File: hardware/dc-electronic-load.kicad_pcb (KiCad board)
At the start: 2 copper layers, 4 parts, among them M1 Mounting Hole, M2 Mounting Hole, M3 Mounting Hole, M4 Mounting Hole

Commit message: more module assigning
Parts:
- added C1: 18pF, klib:CAPC2012X100N, F.Cu at (175.9, 88.4)
- added C10: 0.1uF, klib:CAPC2012X100N, F.Cu at (162.2, 100.4)
- added C11: 0.1uF, klib:CAPC2012X100N, F.Cu at (185.7, 83.4)
- added C12: 0.1uF, klib:CAPC2012X100N, F.Cu at (190.7, 79.1)
- added C13: 0.47uF, klib:CAPC2012X100N, F.Cu at (195.7, 74.0)
- added C14: 0.1uF, klib:CAPC2012X100N, F.Cu at (162.2, 97.8)
- added C15: 0.1uF, klib:CAPC2012X100N, F.Cu at (175.9, 93.6)
- added C16: 0.1uF, klib:CAPC2012X100N, F.Cu at (180.9, 88.4)
- added C17: 0.01uF, klib:CAPC2012X100N, F.Cu at (172.3, 97.8)
- added C18: 0.01uF, klib:CAPC2012X100N, F.Cu at (180.9, 91.0)
- added C19: 0.1uF, klib:CAPC2012X100N, F.Cu at (172.3, 100.4)
- added C2: 18pF, klib:CAPC2012X100N, F.Cu at (175.9, 91.0)
- added C20: 0.1uF, klib:CAPC2012X100N, F.Cu at (195.7, 76.6)
- added C21: 1uF, klib:CAPC2012X100N, F.Cu at (190.7, 81.7)
- added C22: 1uF, klib:CAPC2012X100N, F.Cu at (200.8, 71.4)
- added C23: 100uF, klib:CAPAE660X790N, F.Cu at (165.1, 83.7)
- added C24: 0.1uF, klib:CAPC2012X100N, F.Cu at (200.8, 74.0)
- added C25: 100uF, klib:CAPAE660X790N, F.Cu at (181.6, 74.3)
- added C26: 22nF, klib:CAPC2012X100N, F.Cu at (180.9, 93.6)
- added C27: 0.1uF, klib:CAPC2012X100N, F.Cu at (185.9, 86.0)
- added C3: 10uF, klib:CAPCP2012X100N, F.Cu at (152.0, 98.4)
- added C4: 18pF, klib:CAPC2012X100N, F.Cu at (167.2, 100.4)
- added C5: 18pF, klib:CAPC2012X100N, F.Cu at (185.7, 80.8)
- added C6: 18pF, klib:CAPC2012X100N, F.Cu at (167.2, 97.8)
- added C7: 18pF, klib:CAPC2012X100N, F.Cu at (195.7, 71.4)
- added C8: 10uF, klib:CAPAE660X790N, F.Cu at (154.7, 91.9)
- added C9: 10uF, klib:CAPAE660X790N, F.Cu at (171.5, 74.3)
- added D1: LED, klib:LEDC3216X100N, F.Cu at (157.6, 98.5)
- added M5: Heat Sink, klib:MTGNP565H328Z565P, F.Cu at (180.4, 82.7)
- added R10: 10K, klib:RESC2012X100N, F.Cu at (200.6, 79.2)
- added R11: 10K, klib:RESC2012X100N, F.Cu at (182.1, 96.4)
- added R12: 10K, klib:RESC2012X100N, F.Cu at (190.8, 89.5)
- added R13: 10K, klib:RESC2012X100N, F.Cu at (195.8, 81.8)
- added R14: 10K, klib:RESC2012X100N, F.Cu at (195.7, 79.2)
- added R15: 10K, klib:RESC2012X100N, F.Cu at (182.1, 99.0)
- added R16: 10K, klib:RESC2012X100N, F.Cu at (190.8, 92.1)
- added R17: 10K, klib:RESC2012X100N, F.Cu at (195.8, 87.0)
- added R18: 470R, klib:RESC2012X100N, F.Cu at (185.9, 88.6)
- added R19: 470R, klib:RESC2012X100N, F.Cu at (187.0, 96.4)
- added R2: 100R, klib:RESC2012X100N, F.Cu at (177.3, 96.2)
- added R20: 820, klib:RESC2012X100N, F.Cu at (200.7, 84.4)
- added R21: 470R, klib:RESC2012X100N, F.Cu at (187.0, 99.0)
- added R22: 1K, klib:RESC2012X100N, F.Cu at (195.7, 89.6)
- added R23: 9K1, klib:RESC2012X100N, F.Cu at (200.7, 87.0)
- added R3: 100R, klib:RESC2012X100N, F.Cu at (200.7, 81.8)
- added R34: 10K, klib:RESC2012X100N, F.Cu at (191.9, 94.7)
- added R35: 10K, klib:RESC2012X100N, F.Cu at (195.8, 84.4)
- added R4: 100R, klib:RESC2012X100N, F.Cu at (177.3, 98.8)
- added R5: 50R, klib:RESC2012X100N, F.Cu at (190.9, 84.3)
- added R6: 50R, klib:RESC2012X100N, F.Cu at (185.9, 91.2)
- added R7: 50R, klib:RESC2012X100N, F.Cu at (200.8, 76.6)
- added R8: 50R, klib:RESC2012X100N, F.Cu at (185.9, 93.8)
- added R9: 10K, klib:RESC2012X100N, F.Cu at (190.9, 86.9)
- added X1: 25MHz, klib:XTAL8045X200N, F.Cu at (161.3, 73.0)
- added X2: 32.768kHZ, klib:SOJ550P370X240-4N, F.Cu at (153.2, 75.4)
- added X3: 8MHz, klib:XTAL8045X200N, F.Cu at (154.8, 83.8)
- moved M4 44.9 mm to (190.2, 73.4)
- moved M1 41.4 mm to (173.6, 82.7)
- moved M3 35.9 mm to (163.2, 92.1)
- moved M2 16.6 mm to (170.3, 92.1)

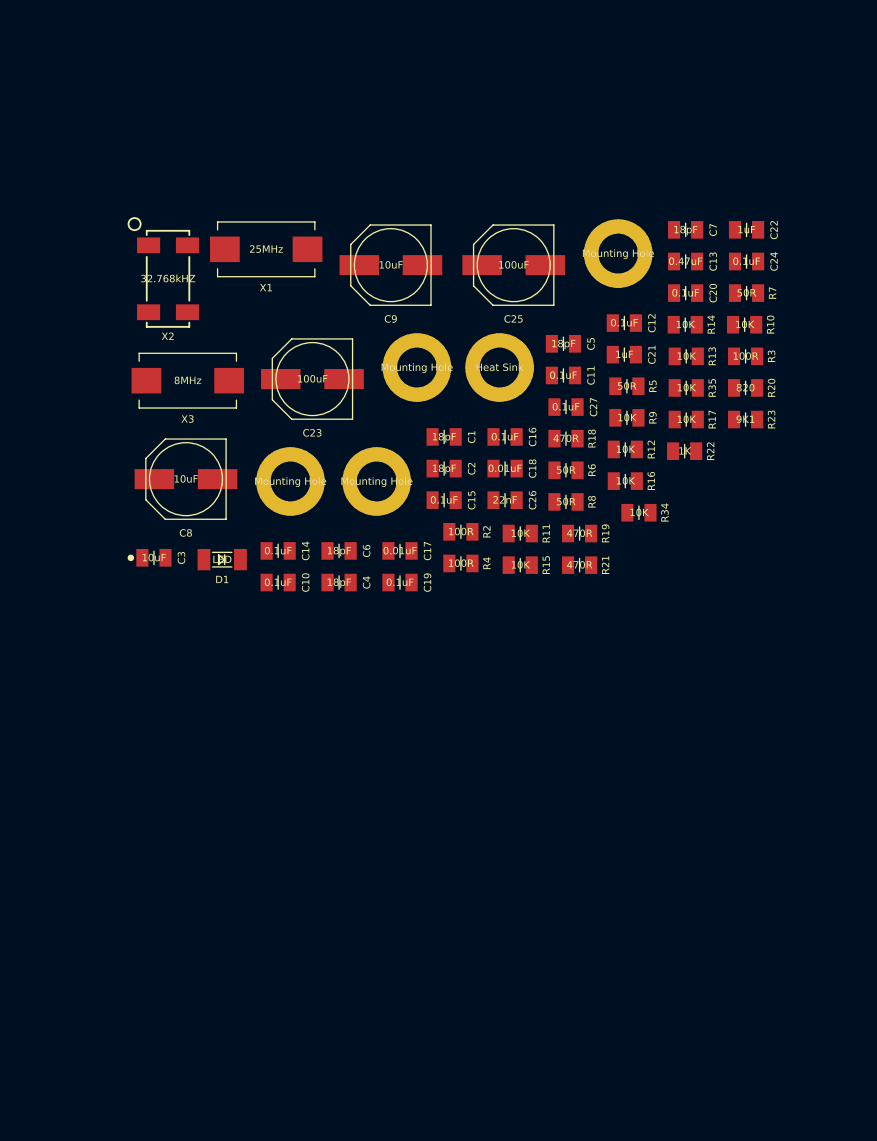
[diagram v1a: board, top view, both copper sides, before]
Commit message: add voltage reg module and resistor module
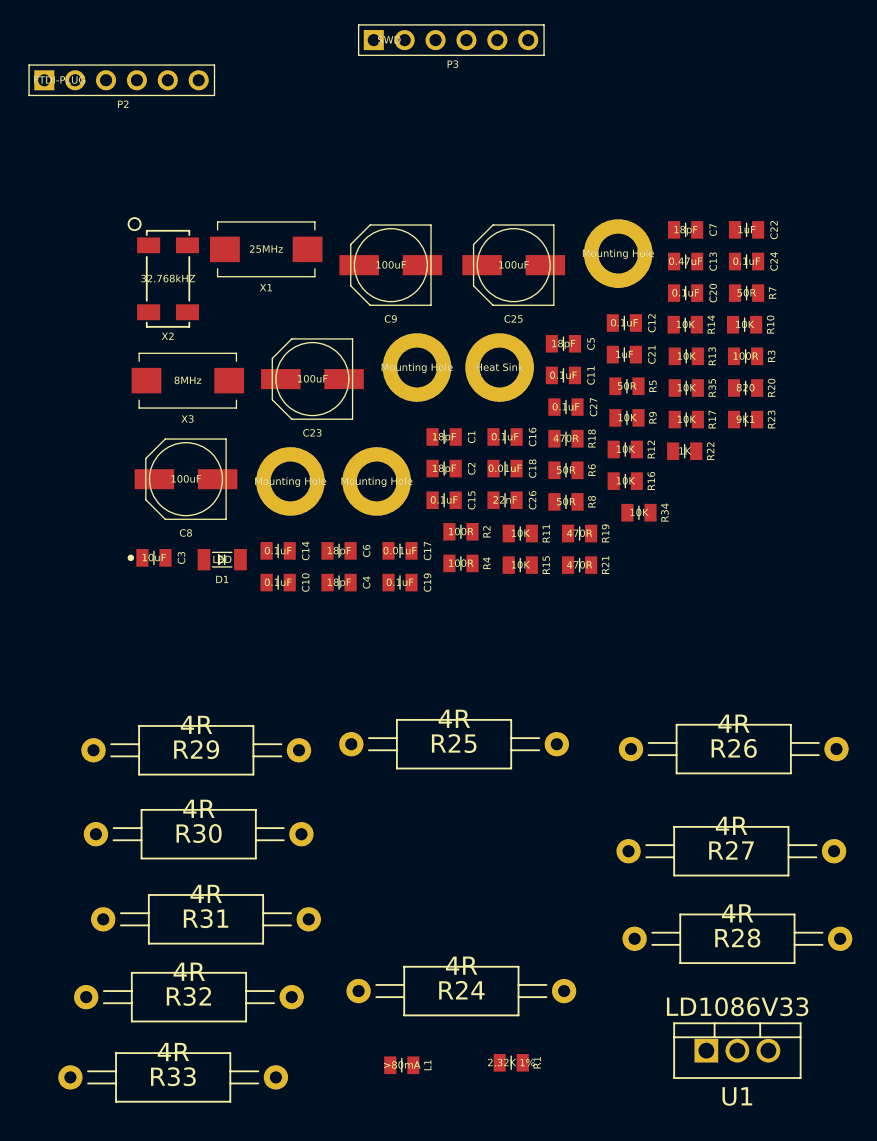
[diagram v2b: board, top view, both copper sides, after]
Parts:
- added L1: >80mA, klib:RESC2012X100N, F.Cu at (172.4, 140.1)
- added M6: Power Entry Connector, klib:EMPTY, F.Cu at (177.4, 126.2)
- added M7: Enclosure (8.36x9.11x3.15), klib:EMPTY, F.Cu at (177.4, 126.2)
- added M8: Fan (50mm x 10mm), klib:EMPTY, F.Cu at (177.4, 126.2)
- added M9: Fan Guard, klib:EMPTY, F.Cu at (177.4, 126.2)
- added P2: FTDI-PLUG, klib:HDRV6W66P254_1X6_1524X249X838P, F.Cu at (143.0, 59.1)
- added P3: SWD, klib:HDRV6W66P254_1X6_1524X249X838P, F.Cu at (170.1, 55.8)
- added P8: FAN, klib:EMPTY, F.Cu at (177.4, 126.2)
- added R1: 2.32K 1%, klib:RESC2012X100N, F.Cu at (181.4, 139.9)
- added R24: 4R, klib:RESAD1690W80L890D400P, F.Cu at (177.3, 134.0)
- added R25: 4R, klib:RESAD1690W80L890D400P, F.Cu at (176.7, 113.7)
- added R26: 4R, klib:RESAD1690W80L890D400P, F.Cu at (199.7, 114.1)
- added R27: 4R, klib:RESAD1690W80L890D400P, F.Cu at (199.5, 122.5)
- added R28: 4R, klib:RESAD1690W80L890D400P, F.Cu at (200.0, 129.7)
- added R29: 4R, klib:RESAD1690W80L890D400P, F.Cu at (155.5, 114.2)
- added R30: 4R, klib:RESAD1690W80L890D400P, F.Cu at (155.7, 121.1)
- added R31: 4R, klib:RESAD1690W80L890D400P, F.Cu at (156.3, 128.1)
- added R32: 4R, klib:RESAD1690W80L890D400P, F.Cu at (154.9, 134.5)
- added R33: 4R, klib:RESAD1690W80L890D400P, F.Cu at (153.6, 141.1)
- added U1: LD1086V33, klib:TO255P460X1020X1925-3P, F.Cu at (200.0, 138.9)
- C8, C9: value 10uF -> 100uF

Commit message: more footprints
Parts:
- added U3: STM32-64PIN, klib:QFP50P1200X1200X160-64N, F.Cu at (208.9, 101.7)

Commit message: more footprints
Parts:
- added U10: TSV631ILT, klib:SOT95P280X100-5N, F.Cu at (227.3, 79.2)
- added U11: BUK954R8-60E,127, klib:TO255P460X1020X1925-3P, F.Cu at (251.8, 76.3)
- added U2: ENC28J60, klib:SOP65P780X200-28N, F.Cu at (247.8, 107.2)
- added U4: TIREF30XX, klib:SOT95P237X112_123-3N, F.Cu at (237.9, 77.7)
- added U5: SST25VF032B-S2A, klib:SOIC127P790X216-8N, F.Cu at (253.2, 96.8)
- added U6: 25AA02EXXX-XOT, klib:SOT95P270X145-6N, F.Cu at (235.8, 112.2)
- added U7: MCP3204, klib:SOIC127P600X175-14N, F.Cu at (227.6, 101.8)
- added U8: MCP49X1, klib:SOP65P490X110-8N, F.Cu at (240.1, 97.4)
- added U9: FQT7N10LTF, klib:SOT230P700X180-4N, F.Cu at (227.5, 88.7)

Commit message: add diode
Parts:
- added D2: DIODE, klib:DIOM5226X220N, F.Cu at (128.2, 95.1)
- added P1: BELFUSE-08B0-1X1T-06-F, klib:BEL-FUSE-08B0-1X1T-06-F, F.Cu at (116.9, 85.0)
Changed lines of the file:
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@@
 (kicad_pcb (version 4) (host pcbnew "(2014-09-04 BZR 5113)-product")
   (general
-    (links 198)
-    (no_connects 198)
+    (links 210)
+    (no_connects 210)
     (area 0 0 0 0)
     (thickness 1.6)
@@
     (tracks 0)
     (zones 0)
-    (modules 90)
+    (modules 92)
     (nets 94)
   )
@@
       (net 40 /ISENSE))
   )
+  (module klib:DIOM5226X220N (layer F.Cu)
+    (at 128.2 95.1)
+    (fp_text reference D2 (at 0 2.286) (layer F.SilkS)
+      (effects (font (size 0.6 0.6) (thickness 0.1)))
+    )
+    (fp_text value DIODE (at 0 0) (layer F.SilkS)
+      (effects (font (size 0.6 0.6) (thickness 0.1)))
+    )
+    (fp_line (start 0.25 -0.5) (end 0.25 0.5) (layer F.SilkS) (width 0.1))
+    (fp_line (start -0.5 -0.5) (end -0.5 0.5) (layer F.SilkS) (width 0.1))
+    (fp_line (start -0.5 0.5) (end 0.25 0) (layer F.SilkS) (width 0.1))
+    (fp_line (start 0.25 0) (end -0.5 -0.5) (layer F.SilkS) (width 0.1))
+    (fp_line (start -3.55 -1.75) (end 3.55 -1.75) (layer Cmts.User) (width 0.1))
+    (fp_line (start 3.55 -1.75) (end 3.55 1.75) (layer Cmts.User) (width 0.1))
+    (fp_line (start 3.55 1.75) (end -3.55 1.75) (layer Cmts.User) (width 0.1))
+    (fp_line (start -3.55 1.75) (end -3.55 -1.75) (layer Cmts.User) (width 0.1))
+    (fp_line (start -2.6 -1.3) (end 2.6 -1.3) (layer F.SilkS) (width 0.1))
+    (fp_line (start 2.6 -1.3) (end 2.6 1.3) (layer F.SilkS) (width 0.1))
+    (fp_line (start 2.6 1.3) (end -2.6 1.3) (layer F.SilkS) (width 0.1))
+    (fp_line (start -2.6 1.3) (end -2.6 -1.3) (layer F.SilkS) (width 0.1))
+    (pad 1 smd rect (at -2.15 0) (size 2.3 1.55) (layers F.Cu F.Paste F.Mask)
+      (net 2 GNDPWR))
+    (pad 2 smd rect (at 2.15 0) (size 2.3 1.55) (layers F.Cu F.Paste F.Mask)
+      (net 93 "Net-(D2-Pad2)"))
+  )
+  (module klib:BEL-FUSE-08B0-1X1T-06-F (layer F.Cu)
+    (at 116.9 85)
+    (fp_text reference P1 (at 0 4.4) (layer F.SilkS)
+      (effects (font (size 0.6 0.6) (thickness 0.1)))
+    )
+    (fp_text value BELFUSE-08B0-1X1T-06-F (at 0 -9.2 90) (layer F.SilkS)
+      (effects (font (size 0.6 0.6) (thickness 0.1)))
+    )
+    (fp_line (start 8.382 -22.098) (end 9.017 -21.463) (layer Cmts.User) (width 0.15))
+    (fp_line (start 7.112 -22.098) (end 9.017 -20.193) (layer Cmts.User) (width 0.15))
+    (fp_line (start 5.588 -22.098) (end 9.017 -18.669) (layer Cmts.User) (width 0.15))
+    (fp_line (start 4.064 -22.098) (end 8.636 -17.526) (layer Cmts.User) (width 0.15))
+    (fp_line (start 2.413 -22.098) (end 6.985 -17.526) (layer Cmts.User) (width 0.15))
+    (fp_line (start 0.762 -22.098) (end 5.334 -17.526) (layer Cmts.User) (width 0.15))
+    (fp_line (start -0.762 -22.098) (end 3.81 -17.526) (layer Cmts.User) (width 0.15))
+    (fp_line (start -2.286 -22.098) (end 2.286 -17.526) (layer Cmts.User) (width 0.15))
+    (fp_line (start -3.81 -22.098) (end 0.762 -17.526) (layer Cmts.User) (width 0.15))
+    (fp_line (start -5.334 -22.098) (end -0.762 -17.526) (layer Cmts.User) (width 0.15))
+    (fp_line (start -6.731 -22.098) (end -2.159 -17.526) (layer Cmts.User) (width 0.15))
+    (fp_line (start -8.255 -22.098) (end -3.683 -17.526) (layer Cmts.User) (width 0.15))
+    (fp_line (start -9.017 -21.59) (end -4.953 -17.526) (layer Cmts.User) (width 0.15))
+    (fp_line (start -9.017 -20.32) (end -6.223 -17.526) (layer Cmts.User) (width 0.15))
+    (fp_line (start -9.017 -18.923) (end -7.62 -17.526) (layer Cmts.User) (width 0.15))
+    (fp_line (start 5.461 -1.905) (end 6.731 -0.635) (layer Cmts.User) (width 0.15))
+    (fp_line (start 5.461 -3.048) (end 7.874 -0.635) (layer Cmts.User) (width 0.15))
+    (fp_line (start 8.001 -4.318) (end 9.017 -3.302) (layer Cmts.User) (width 0.15))
+    (fp_line (start 6.731 -4.318) (end 9.017 -2.032) (layer Cmts.User) (width 0.15))
+    (fp_line (start 5.461 -4.318) (end 9.017 -0.762) (layer Cmts.User) (width 0.15))
+    (fp_line (start -9.017 -1.778) (end -7.874 -0.635) (layer Cmts.User) (width 0.15))
+    (fp_line (start -9.017 -3.048) (end -6.604 -0.635) (layer Cmts.User) (width 0.15))
+    (fp_line (start -9.017 -4.318) (end -5.461 -0.762) (layer Cmts.User) (width 0.15))
+    (fp_line (start -6.731 -4.318) (end -5.461 -3.175) (layer Cmts.User) (width 0.15))
+    (fp_line (start -7.874 -4.318) (end -5.461 -1.905) (layer Cmts.User) (width 0.15))
+    (fp_line (start -11.43 -22.098) (end -11.43 6.35) (layer Cmts.User) (width 0.15))
+    (fp_line (start -11.43 6.35) (end 11.43 6.35) (layer Cmts.User) (width 0.15))
+    (fp_line (start 11.43 6.35) (end 11.43 -22.098) (layer Cmts.User) (width 0.15))
+    (fp_line (start -8.1534 -22.098) (end 8.1534 -22.098) (layer F.SilkS) (width 0.15))
+    (fp_line (start 8.1534 -22.098) (end 8.1534 3.429) (layer F.SilkS) (width 0.15))
+    (fp_line (start 8.1534 3.429) (end -8.1534 3.429) (layer F.SilkS) (width 0.15))
+    (fp_line (start -8.1534 3.429) (end -8.1534 -22.098) (layer F.SilkS) (width 0.15))
+    (fp_line (start 5.461 -0.635) (end 5.461 -4.318) (layer Cmts.User) (width 0.15))
+    (fp_line (start 5.461 -0.635) (end 9.017 -0.635) (layer Cmts.User) (width 0.15))
+    (fp_line (start 9.017 -4.318) (end 9.017 -0.635) (layer Cmts.User) (width 0.15))
+    (fp_line (start 9.017 -4.318) (end 5.461 -4.318) (layer Cmts.User) (width 0.15))
+    (fp_line (start -9.017 -4.318) (end -5.461 -4.318) (layer Cmts.User) (width 0.15))
+    (fp_line (start -5.461 -4.318) (end -5.461 -0.635) (layer Cmts.User) (width 0.15))
+    (fp_line (start -5.461 -0.635) (end -9.017 -0.635) (layer Cmts.User) (width 0.15))
+    (fp_line (start -9.017 -0.635) (end -9.017 -4.318) (layer Cmts.User) (width 0.15))
+    (fp_line (start -9.017 -22.098) (end 9.017 -22.098) (layer Cmts.User) (width 0.15))
+    (fp_line (start 9.017 -22.098) (end 9.017 -17.526) (layer Cmts.User) (width 0.15))
+    (fp_line (start -9.017 -17.526) (end 9.017 -17.526) (layer Cmts.User) (width 0.15))
+    (fp_line (start -9.017 -17.526) (end -9.017 -22.098) (layer Cmts.User) (width 0.15))
+    (pad 1 thru_hole circle (at -5.08 0) (size 1.524 1.524) (drill 1.016) (layers *.Cu *.Mask F.SilkS)
+      (net 11 "Net-(C10-Pad1)"))
+    (pad 2 thru_hole circle (at -3.048 0) (size 1.524 1.524) (drill 1.016) (layers *.Cu *.Mask F.SilkS)
+      (net 24 "Net-(P1-Pad2)"))
+    (pad 3 thru_hole circle (at -1.016 0) (size 1.524 1.524) (drill 1.016) (layers *.Cu *.Mask F.SilkS)
+      (net 25 "Net-(P1-Pad3)"))
+    (pad 4 thru_hole circle (at 1.016 0) (size 1.524 1.524) (drill 1.016) (layers *.Cu *.Mask F.SilkS)
+      (net 26 "Net-(P1-Pad4)"))
+    (pad 5 thru_hole circle (at 3.048 0) (size 1.524 1.524) (drill 1.016) (layers *.Cu *.Mask F.SilkS)
+      (net 27 "Net-(P1-Pad5)"))
+    (pad 6 thru_hole circle (at 5.08 0) (size 1.524 1.524) (drill 1.016) (layers *.Cu *.Mask F.SilkS)
+      (net 12 "Net-(C11-Pad1)"))
+    (pad 7 thru_hole circle (at -7.2136 2.4638) (size 1.651 1.651) (drill 1.143) (layers *.Cu *.Mask F.SilkS)
+      (net 2 GNDPWR))
+    (pad 8 thru_hole circle (at -4.6736 2.4638) (size 1.651 1.651) (drill 1.143) (layers *.Cu *.Mask F.SilkS)
+      (net 20 "Net-(P1-Pad8)"))
+    (pad 9 thru_hole circle (at 4.6736 2.4638) (size 1.651 1.651) (drill 1.143) (layers *.Cu *.Mask F.SilkS)
+      (net 2 GNDPWR))
+    (pad 10 thru_hole circle (at 7.2136 2.4638) (size 1.651 1.651) (drill 1.143) (layers *.Cu *.Mask F.SilkS)
+      (net 22 "Net-(P1-Pad10)"))
+    (pad "" thru_hole circle (at 6.35 -11.176) (size 3.302 3.302) (drill 3.2512) (layers *.Cu *.Mask F.SilkS))
+    (pad "" thru_hole circle (at -6.35 -11.176) (size 3.302 3.302) (drill 3.2512) (layers *.Cu *.Mask F.SilkS))
+    (pad "" thru_hole circle (at -8.0645 -14.351) (size 1.651 1.651) (drill 1.5748) (layers *.Cu *.Mask F.SilkS))
+    (pad "" thru_hole circle (at 8.0645 -14.351) (size 1.651 1.651) (drill 1.5748) (layers *.Cu *.Mask F.SilkS))
+  )
 )

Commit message: resistors
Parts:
- D2: value DIODE -> GS1M-LTP
- M5: value Heat Sink -> Heat Sink (RA-T2X-38E); footprint klib:MTGNP565H328Z565P -> klib:OHMITE-R-SERIES
- moved M5 82.4 mm to (106.7, 119.4)
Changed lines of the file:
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@@
-(kicad_pcb (version 4) (host pcbnew "(2014-09-04 BZR 5113)-product")
+(kicad_pcb (version 4) (host pcbnew "(2014-09-11 BZR 5128)-product")
   (general
     (links 210)
@@
       (net 19 "Net-(D1-Pad2)"))
   )
-  (module klib:MTGNP565H328Z565P (layer F.Cu)
-    (at 180.444001 82.724001)
-    (fp_text reference M5 (at 0 3.683) (layer F.SilkS) hide
-      (effects (font (size 0.6 0.6) (thickness 0.1)))
-    )
-    (fp_text value "Heat Sink" (at 0 0) (layer F.SilkS)
-      (effects (font (size 0.6 0.6) (thickness 0.1)))
-    )
-    (fp_circle (center 0 0) (end 2.95 0) (layer Cmts.User) (width 0.1))
-    (pad "" thru_hole circle (at 0 0) (size 5.65 5.65) (drill 3.2766) (layers *.Cu *.Mask F.SilkS))
-  )
   (module klib:RESC2012X100N (layer F.Cu)
     (at 177.264001 96.234001)
@@
       (effects (font (size 0.6 0.6) (thickness 0.1)))
     )
-    (fp_text value DIODE (at 0 0) (layer F.SilkS)
+    (fp_text value GS1M-LTP (at 0 0) (layer F.SilkS)
       (effects (font (size 0.6 0.6) (thickness 0.1)))
     )
@@
     (pad "" thru_hole circle (at 8.0645 -14.351) (size 1.651 1.651) (drill 1.5748) (layers *.Cu *.Mask F.SilkS))
   )
+  (module klib:OHMITE-R-SERIES (layer F.Cu)
+    (at 106.68 119.38)
+    (fp_text reference M5 (at 0 7.62) (layer F.SilkS)
+      (effects (font (size 1.5 1.5) (thickness 0.15)))
+    )
+    (fp_text value "Heat Sink (RA-T2X-38E)" (at 0 -7.62) (layer F.SilkS)
+      (effects (font (size 1.5 1.5) (thickness 0.15)))
+    )
+    (fp_line (start 0 0) (end 0 -1.27) (layer F.SilkS) (width 0.15))
+    (fp_line (start 1.8 -2) (end 1.8 0) (layer F.SilkS) (width 0.15))
+    (fp_line (start -1.8 -2) (end -1.8 0) (layer F.SilkS) (width 0.15))
+    (fp_line (start 12.5 3.81) (end 12.5 12.5) (layer F.SilkS) (width 0.15))
+    (fp_line (start 12.5 12.5) (end 21 12.5) (layer F.SilkS) (width 0.15))
+    (fp_line (start 21 12.5) (end 21 -12.5) (layer F.SilkS) (width 0.15))
+    (fp_line (start 21 -12.5) (end 6 -12.5) (layer F.SilkS) (width 0.15))
+    (fp_line (start 6 -12.5) (end 6 -2) (layer F.SilkS) (width 0.15))
+    (fp_line (start 6 -2) (end -6 -2) (layer F.SilkS) (width 0.15))
+    (fp_line (start -6 -2) (end -6 -12.5) (layer F.SilkS) (width 0.15))
+    (fp_line (start -6 -12.5) (end -21 -12.5) (layer F.SilkS) (width 0.15))
+    (fp_line (start -21 -12.5) (end -21 12.5) (layer F.SilkS) (width 0.15))
+    (fp_line (start -21 12.5) (end -12.5 12.5) (layer F.SilkS) (width 0.15))
+    (fp_line (start -12.5 12.5) (end -12.5 3.81) (layer F.SilkS) (width 0.15))
+    (fp_line (start -8.69 0) (end 8.69 0) (layer F.SilkS) (width 0.15))
+    (pad 1 thru_hole circle (at -12.7 0) (size 5.4 5.4) (drill 2.4) (layers *.Cu *.Mask F.SilkS))
+    (pad 2 thru_hole circle (at 12.7 0) (size 5.4 5.4) (drill 2.4) (layers *.Cu *.Mask F.SilkS))
+  )
 )
